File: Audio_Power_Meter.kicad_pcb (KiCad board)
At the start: 2 copper layers, 32 x 70 mm, 23 parts, among them P1 AMP, P2 CONN_01X01, P3 power, U1 LM3915

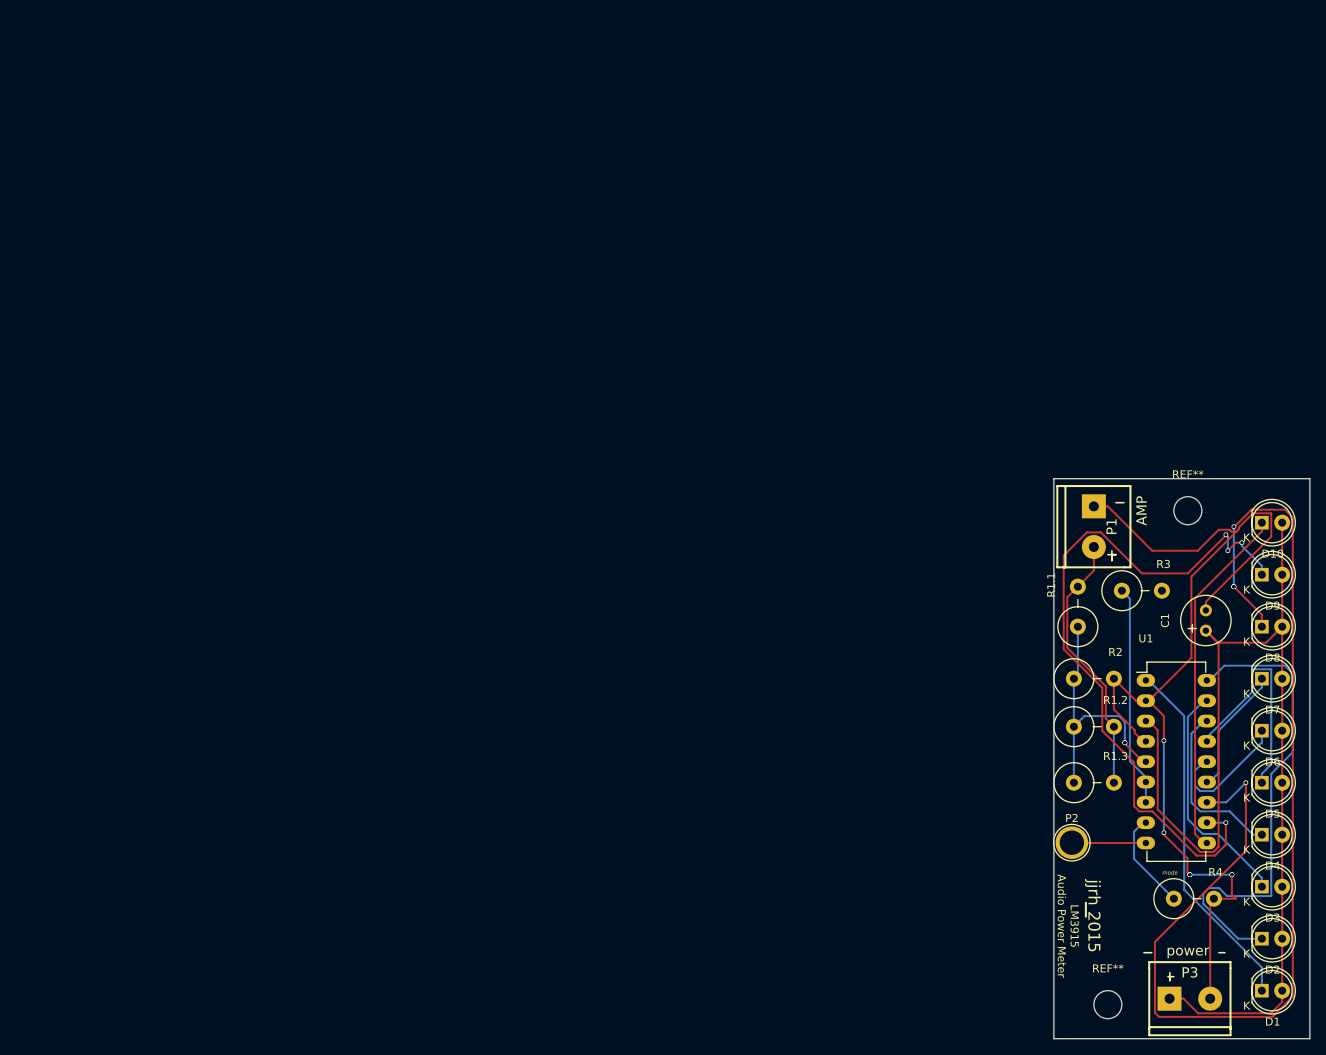
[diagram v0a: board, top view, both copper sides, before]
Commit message: made pcb page size smaller for exporty
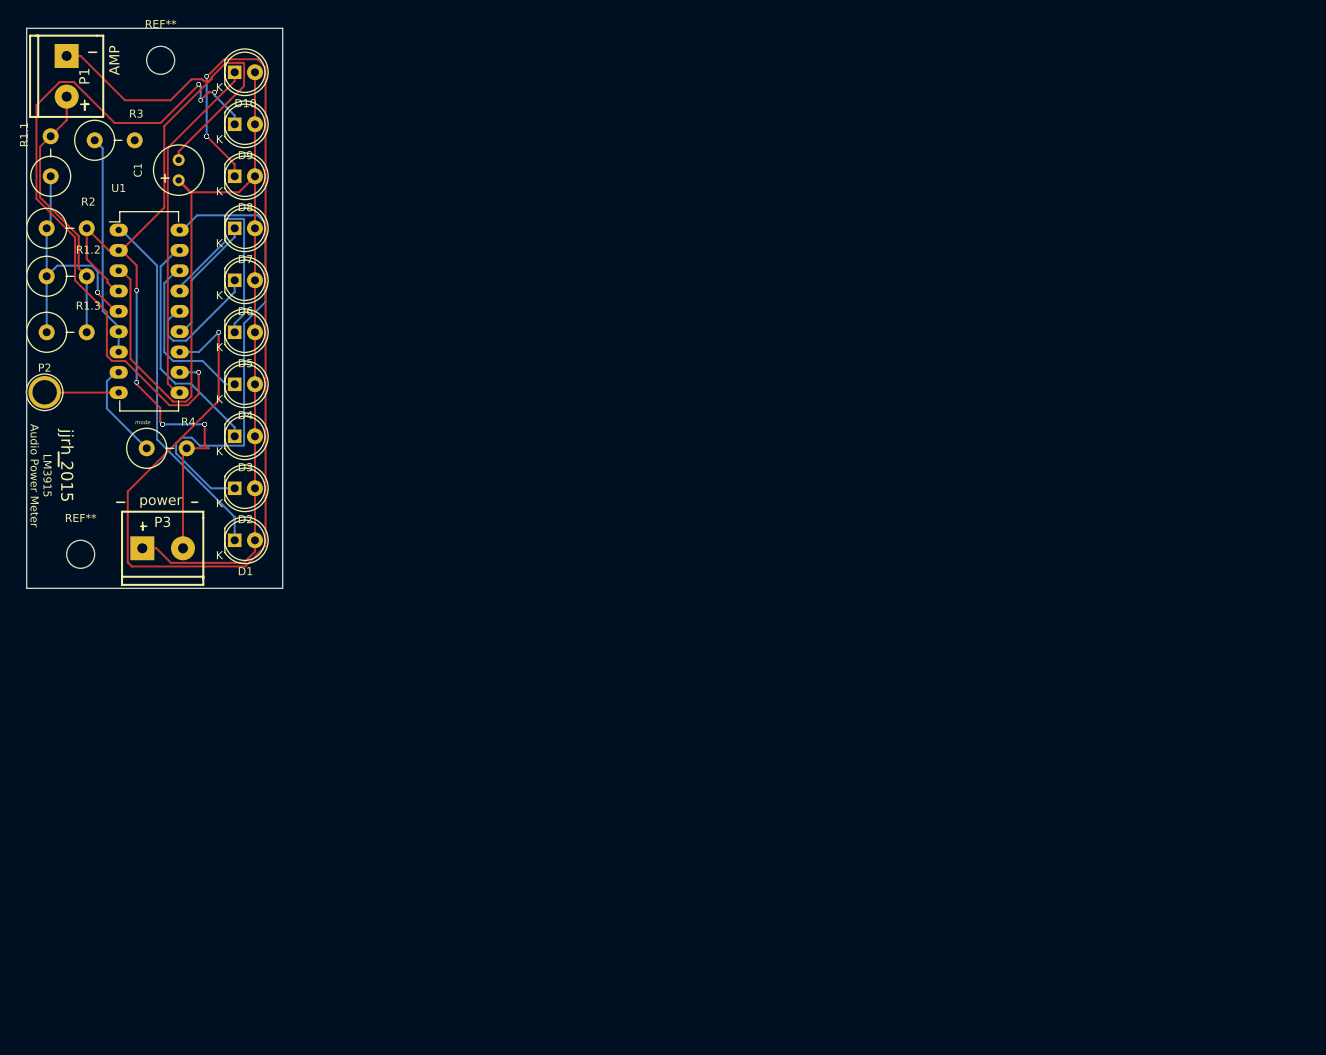
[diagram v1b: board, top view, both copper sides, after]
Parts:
- moved C1 140.2 mm to (56.6, 34.7)
- moved D1 140.2 mm to (63.6, 79.7)
- moved D10 140.2 mm to (63.6, 21.2)
- moved D2 140.2 mm to (63.6, 73.2)
- moved D3 140.2 mm to (63.6, 66.7)
- moved D4 140.2 mm to (63.6, 60.2)
- moved D5 140.2 mm to (63.6, 53.7)
- moved D6 140.2 mm to (63.6, 47.2)
- moved D7 140.2 mm to (63.6, 40.7)
- moved D8 140.2 mm to (63.6, 34.2)
- moved D9 140.2 mm to (63.6, 27.7)
- moved P1 140.2 mm to (42.6, 21.7)
- moved P2 140.2 mm to (39.9, 61.2)
- moved P3 140.2 mm to (54.6, 80.7)
- moved R1.1 140.2 mm to (40.6, 31.7)
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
